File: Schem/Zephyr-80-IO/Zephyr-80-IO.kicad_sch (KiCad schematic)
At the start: 0 parts

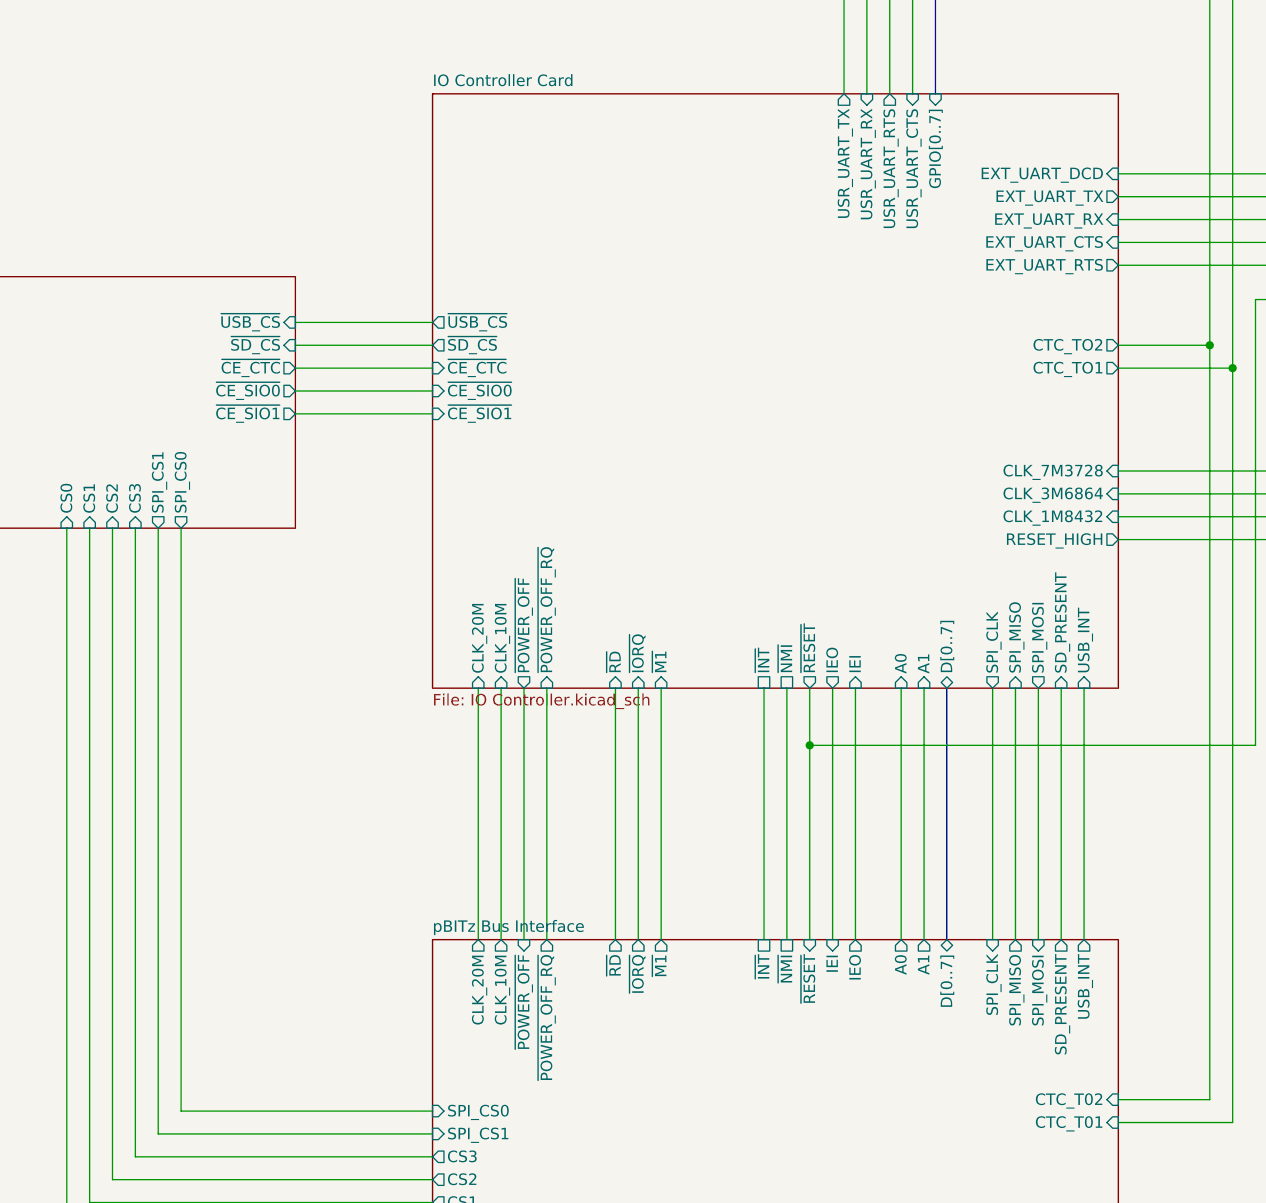
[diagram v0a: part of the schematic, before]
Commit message: Completed the IO Controller schematic and PCB layout for the Zephyr-80 project. This includes the design of the Baud Clock, CPU Address Decoding, Console Port, Device Select Decode, GPIO User Serial, and the main IO Controller schematics. Additionally, the PCB layout for the Zephyr-80 IO board has been created, along with the necessary library files and documentation for the control signal mapping.
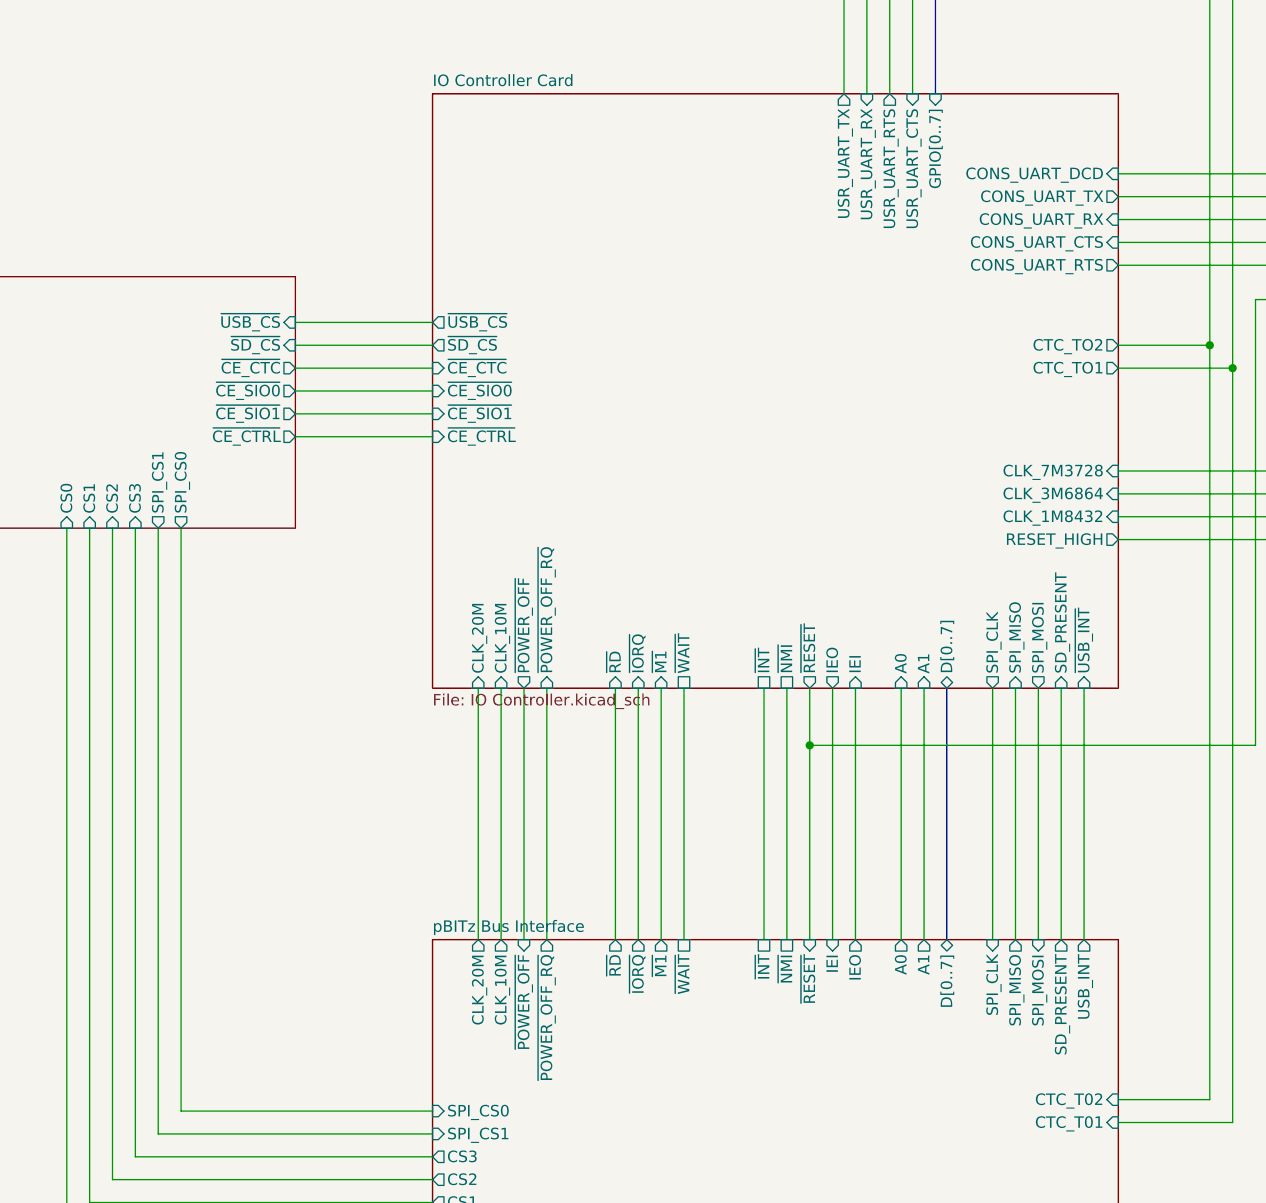
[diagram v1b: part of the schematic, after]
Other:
- sheet Device Select Decode ports: added ~{CE_CTRL}; removed none
- sheet IO Controller Card ports: added CONS_UART_CTS, CONS_UART_DCD, CONS_UART_RTS, CONS_UART_RX, CONS_UART_TX, ~{CE_CTRL}, ~{USB_INT}, ~{WAIT}; removed EXT_UART_CTS, EXT_UART_DCD, EXT_UART_RTS, EXT_UART_RX, EXT_UART_TX, USB_INT
- sheet pBITz Bus Interface ports: added ~{WAIT}; removed none
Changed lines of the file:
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@@
+	(wire
+		(pts
+			(xy 276.86 168.91) (xy 292.1 168.91)
+		)
+		(stroke
+			(width 0)
+			(type default)
+		)
+	)
 	(wire
 		(pts
@@
 		(pts
 			(xy 254 254) (xy 254 179.07)
+		)
+		(stroke
+			(width 0)
+			(type default)
+		)
+	)
+	(wire
+		(pts
+			(xy 320.04 196.85) (xy 320.04 224.79)
 		)
 		(stroke
@@
 			)
 		)
+		(pin "~{CE_CTRL}" output
+			(at 276.86 168.91 0)
+			(effects
+				(font
+					(size 1.27 1.27)
+				)
+				(justify right)
+			)
+		)
 		(instances
 			(project "Zephyr-80-IO"
@@
 			)
 		)
-		(pin "EXT_UART_RTS" output
-			(at 368.3 149.86 0)
-			(effects
-				(font
-					(size 1.27 1.27)
-				)
-				(justify right)
-			)
-		)
-		(pin "EXT_UART_RX" input
-			(at 368.3 144.78 0)
-			(effects
-				(font
-					(size 1.27 1.27)
-				)
-				(justify right)
-			)
-		)
 		(pin "SPI_MISO" input
 			(at 356.87 196.85 270)
@@
 			)
 		)
-		(pin "EXT_UART_CTS" input
-			(at 368.3 147.32 0)
-			(effects
-				(font
-					(size 1.27 1.27)
-				)
-				(justify right)
-			)
-		)
 		(pin "USR_UART_TX" output
 			(at 337.82 130.81 90)
@@
 			)
 		)
-		(pin "EXT_UART_TX" output
-			(at 368.3 142.24 0)
-			(effects
-				(font
-					(size 1.27 1.27)
-				)
-				(justify right)
-			)
-		)
 		(pin "IEO" output
 			(at 336.55 196.85 270)
@@
 			)
 		)
-		(pin "EXT_UART_DCD" input
-			(at 368.3 139.7 0)
-			(effects
-				(font
-					(size 1.27 1.27)
-				)
-				(justify right)
-			)
-		)
 		(pin "~{POWER_OFF_RQ}" input
 			(at 304.8 196.85 270)
@@
 			)
 		)
-		(pin "USB_INT" input
-			(at 364.49 196.85 270)
-			(effects
-				(font
-					(size 1.27 1.27)
-				)
-				(justify left)
-			)
-		)
 		(pin "A0" input
 			(at 344.17 196.85 270)
@@
 				)
 				(justify left)
+			)
+		)
+		(pin "CONS_UART_RTS" output
+			(at 368.3 149.86 0)
+			(effects
+				(font
+					(size 1.27 1.27)
+				)
+				(justify right)
+			)
+		)
+		(pin "CONS_UART_CTS" input
+			(at 368.3 147.32 0)
+			(effects
+				(font
+					(size 1.27 1.27)
+				)
+				(justify right)
+			)
+		)
+		(pin "CONS_UART_TX" output
+			(at 368.3 142.24 0)
+			(effects
+				(font
+					(size 1.27 1.27)
+				)
+				(justify right)
+			)
+		)
+		(pin "CONS_UART_DCD" input
+			(at 368.3 139.7 0)
+			(effects
+				(font
+					(size 1.27 1.27)
+				)
+				(justify right)
+			)
+		)
+		(pin "~{USB_INT}" input
+			(at 364.49 196.85 270)
+			(effects
+				(font
+					(size 1.27 1.27)
+				)
+				(justify left)
+			)
+		)
+		(pin "~{CE_CTRL}" input
+			(at 292.1 168.91 180)
+			(effects
+				(font
+					(size 1.27 1.27)
+				)
+				(justify left)
+			)
+		)
+		(pin "~{WAIT}" passive
+			(at 320.04 196.85 270)
+			(effects
+				(font
+					(size 1.27 1.27)
+				)
+				(justify left)
+			)
+		)
+		(pin "CONS_UART_RX" input
+			(at 368.3 144.78 0)
+			(effects
+				(font
+					(size 1.27 1.27)
+				)
+				(justify right)
 			)
 		)
@@
 			(effects
 				(font
+					(size 1.27 1.27)
+				)
+				(justify right)
+			)
+		)
+		(pin "~{WAIT}" passive
+			(at 320.04 224.79 90)
+			(effects
+				(font
